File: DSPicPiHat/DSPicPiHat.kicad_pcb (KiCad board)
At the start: 2 copper layers, 65 x 66.5 mm, 85 parts, among them J1 Conn_01x09_Female, J4 Conn_PIC_ICSP_ICD, J5 USB_C_Receptacle_USB2.0, J6 PowerInput, J8 RasPiHeaders, SW1 POWER_Select, SW2 SW_DIP_x08, U1 DSPIC33CH512MP508T-I_PT, U10 DF5A6.2CJE_LM, U11 FT230XS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

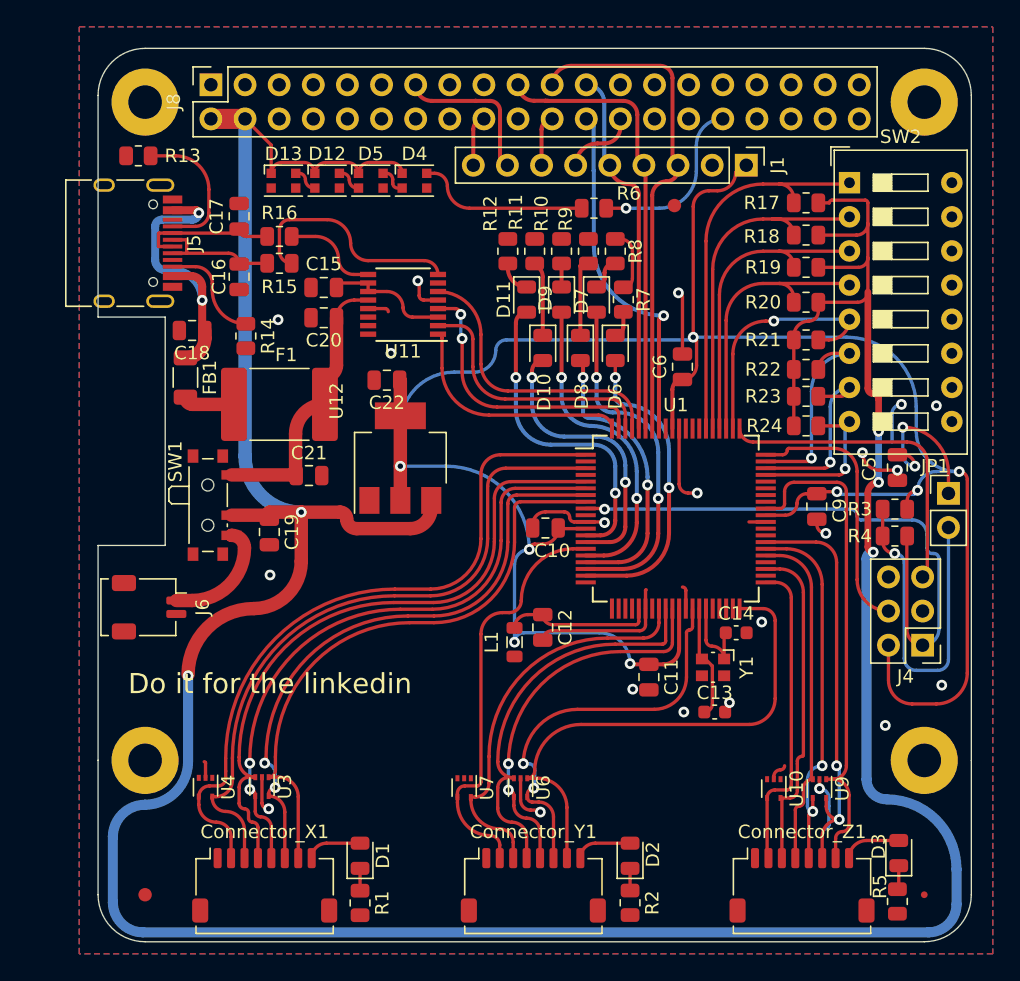
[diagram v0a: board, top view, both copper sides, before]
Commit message: Rounded some comers and added more pcb art
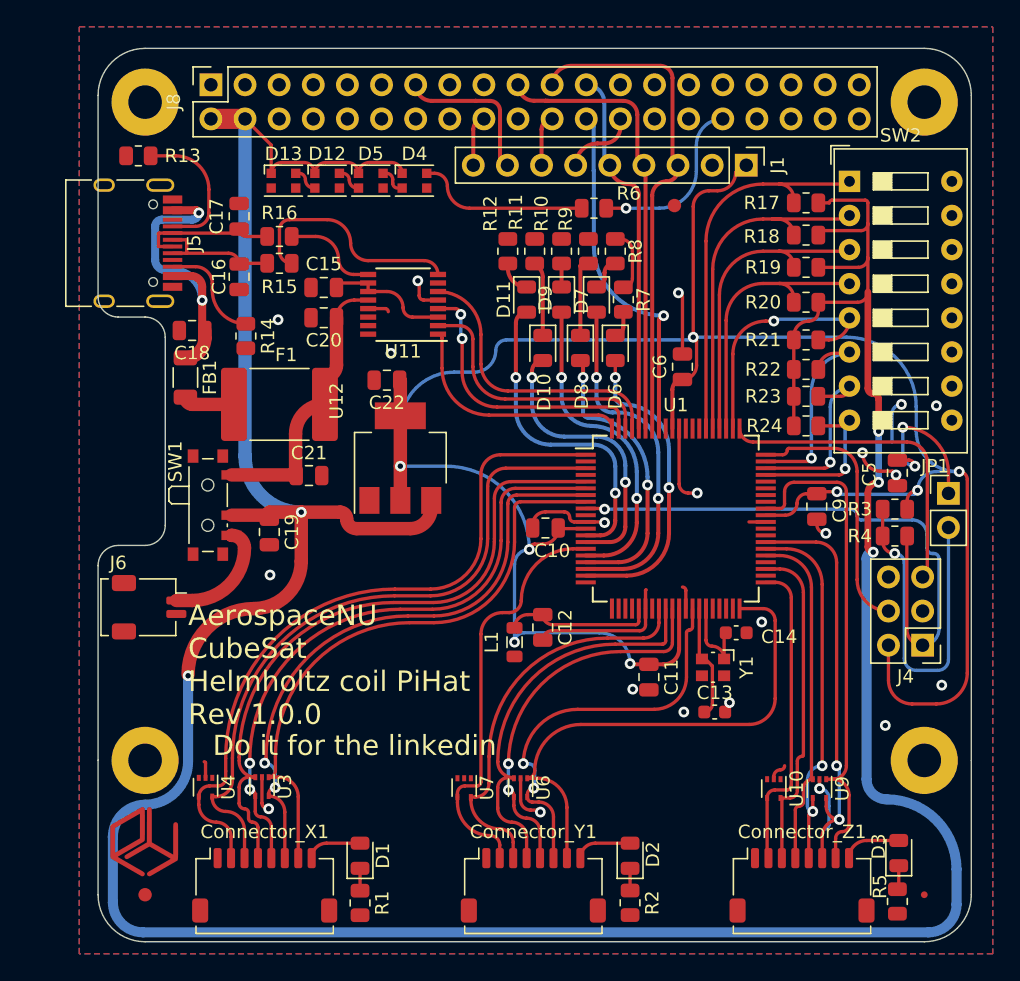
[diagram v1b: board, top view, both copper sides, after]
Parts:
- added G*** (x2): LOGO, footprints:SmallLogo, F.Cu at (60.0, 132.5)
- added G***: LOGO, footprints:Banner, B.Cu at (89.7, 134.0)
- moved C5 0.40 mm to (116.0, 105.1)
- moved SW2 0.10 mm to (112.4, 83.4)
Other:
- outline, holes or cut-outs redrawn
- board text added: "AerospaceNU CubeSat Helmholtz coil PiHat Rev 1.0.0"

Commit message: Grounded mounting points
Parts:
- removed ?: , 
- removed the REF** at (118.0, 77.5)
- removed the REF** at (60.0, 77.5)
- removed the REF** at (60.0, 126.5)
- added H1: MountingHole_Pad, MountingHole:MountingHole_2.7mm_M2.5_DIN965_Pad, F.Cu at (60.0, 77.5)
- added H2: MountingHole_Pad, MountingHole:MountingHole_2.7mm_M2.5_DIN965_Pad, F.Cu at (60.0, 126.5)
- added H3: MountingHole_Pad, MountingHole:MountingHole_2.7mm_M2.5_DIN965_Pad, F.Cu at (118.0, 126.5)
- added H4: MountingHole_Pad, MountingHole:MountingHole_2.7mm_M2.5_DIN965_Pad, F.Cu at (118.0, 77.5)
- moved C5 0.25 mm to (116.0, 105.3)
- moved R3 0.20 mm to (115.8, 108.0)
- moved R4 0.20 mm to (115.8, 110.0)

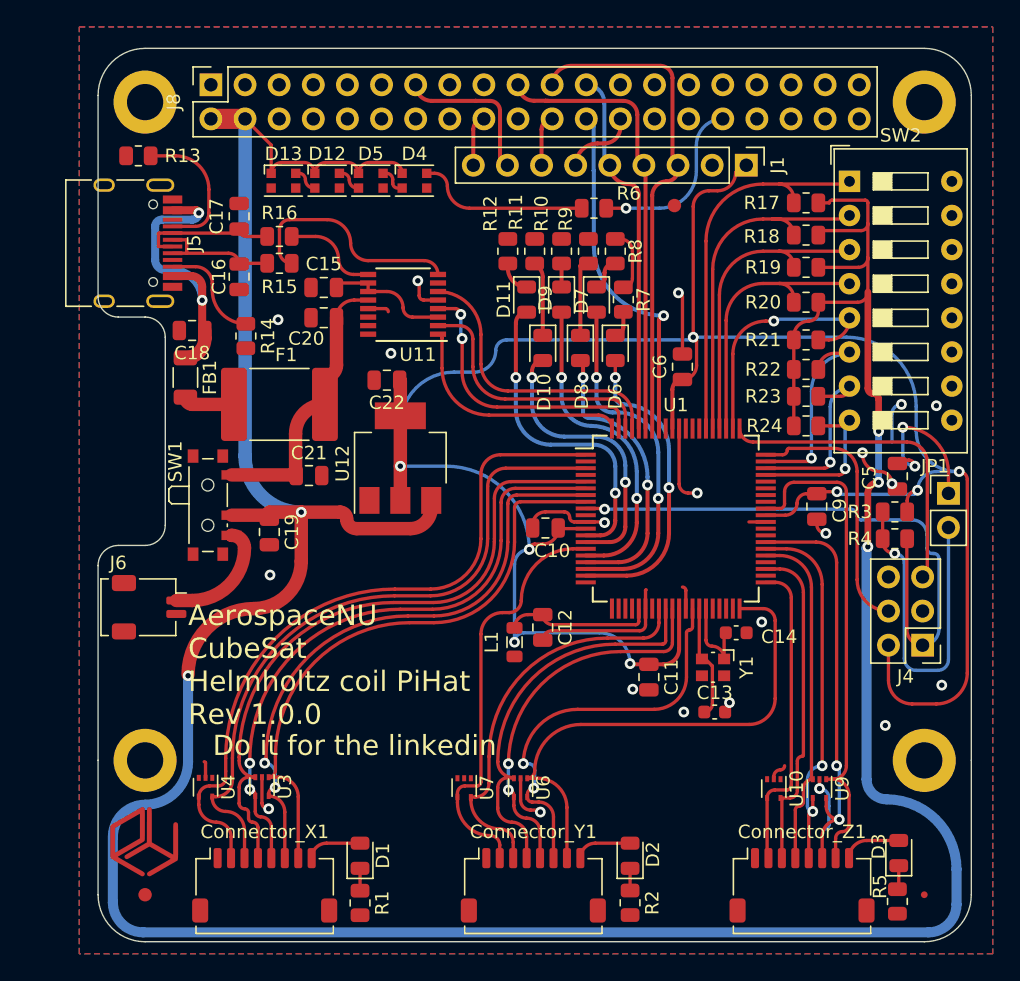
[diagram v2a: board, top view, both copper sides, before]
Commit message: Fixed pi header connections
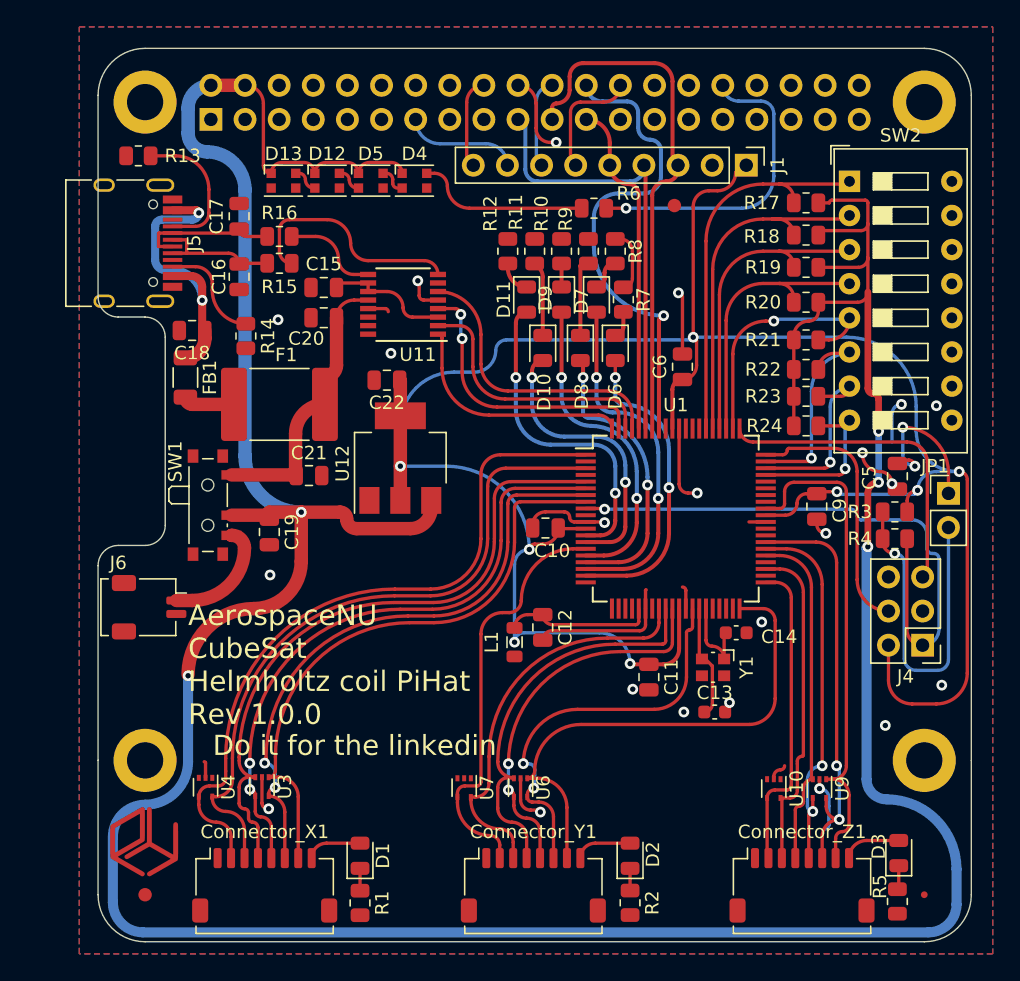
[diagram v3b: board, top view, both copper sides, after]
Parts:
- J8: moved to B.Cu
- moved J8 2.58 mm to (64.9, 78.8), turned to -90 degrees
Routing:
- net PI_NEOPIXEL: track 13.1 -> 23.3 mm
- net PI_CE0: track 26.2 -> 35.9 mm
- net +5V: track 252.7 -> 261.1 mm
- net AVSS: track 61.3 -> 67.2 mm, vias 21 -> 22
- net PI_CE1: track 5.45 -> 8.93 mm
- net Backlight: track 3.87 -> 6.89 mm
- net RST: track 11.6 -> 8.64 mm
- net Data/Command: track 3.87 -> 6.78 mm
- net PI_MISO: track 36.7 -> 39.0 mm
- net PI_SCLK: track 27.7 -> 26.5 mm

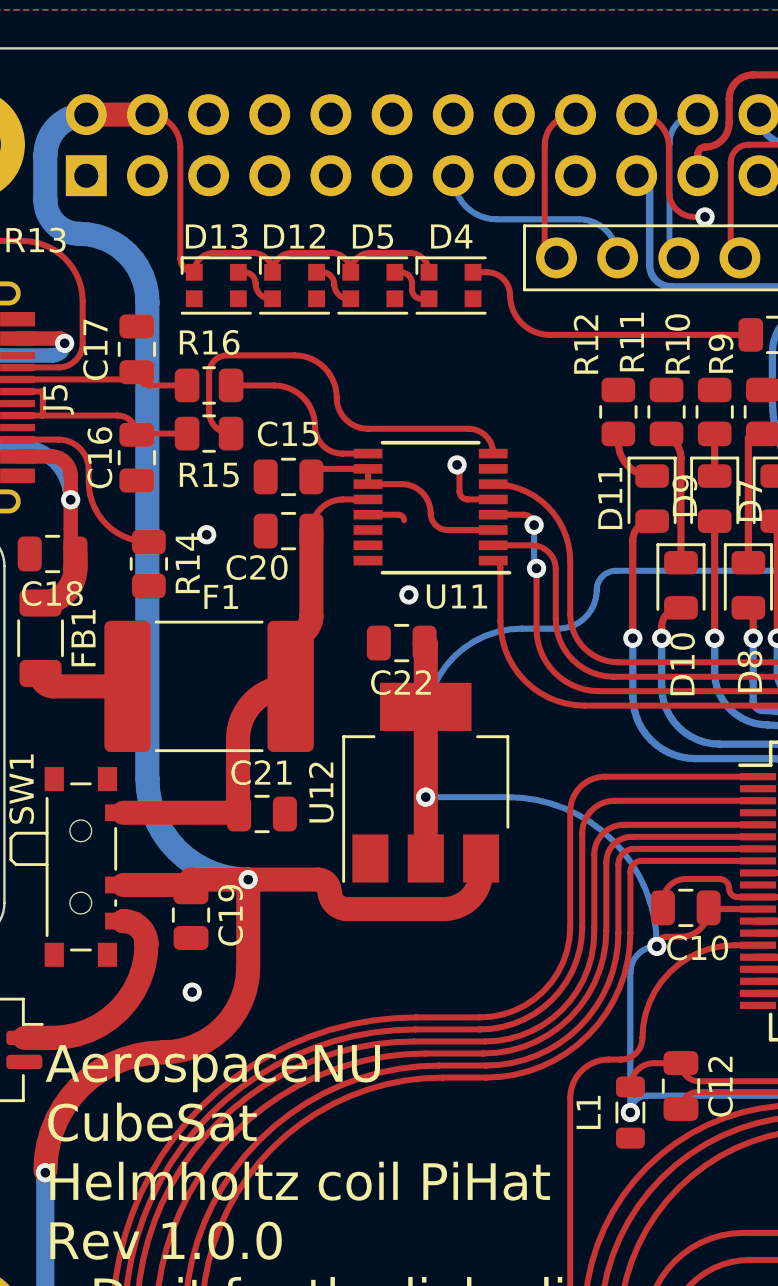
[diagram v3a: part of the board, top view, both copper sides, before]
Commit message: Moved fuse to be after the PSU switch
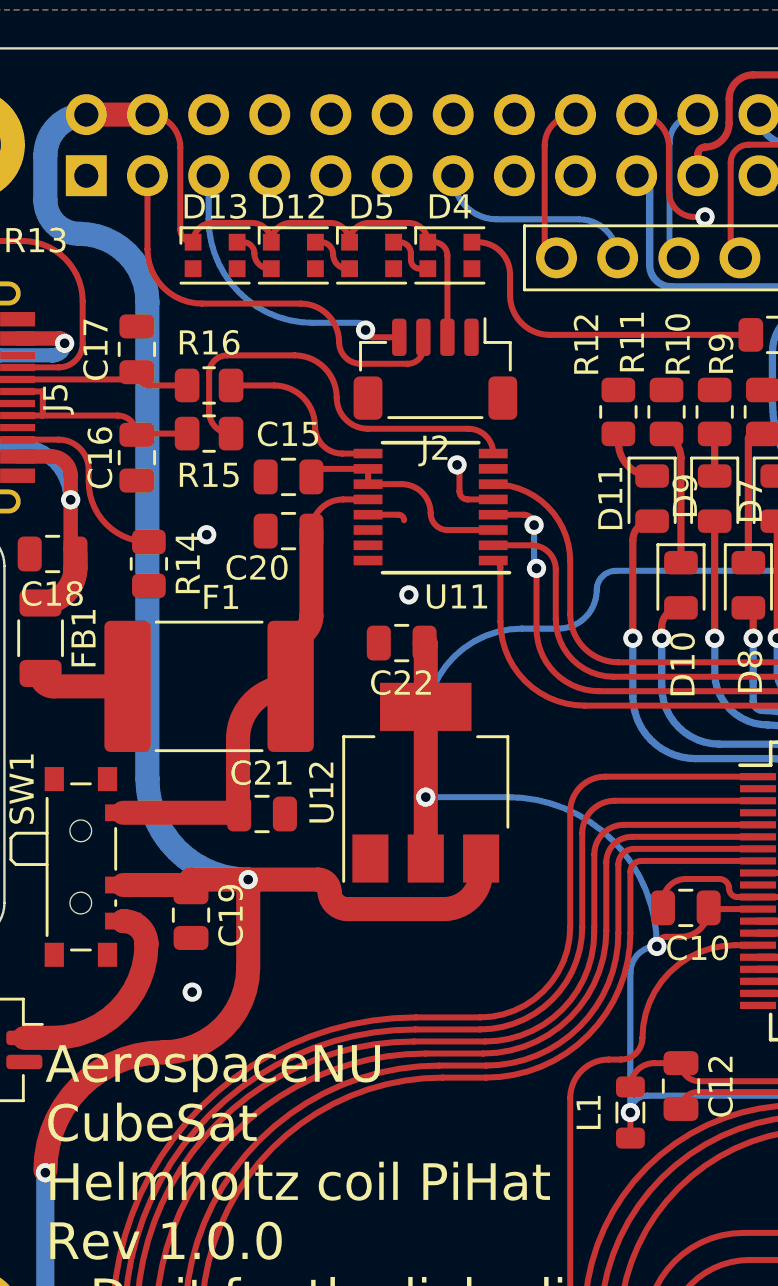
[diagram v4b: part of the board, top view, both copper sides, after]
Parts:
- added J2: Conn_01x04_Female, Connector_JST:JST_SH_BM04B-SRSS-TB_1x04-1MP_P1.00mm_Vertical, F.Cu at (79.4, 86.8)
- L1: value 10 mA <1o -> 6.33 mH
- moved D12 1.25 mm to (73.5, 82.1)
- moved D13 1.25 mm to (70.2, 82.1)
- moved D4 1.25 mm to (80.0, 82.1)
- moved D5 1.25 mm to (76.8, 82.1)
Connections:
- J8 pad 3: unconnected-(J8-Pad3) -> PI_I2C_SDA
- J8 pad 5: unconnected-(J8-Pad5) -> PI_I2C_SCL
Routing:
- net PI_I2C_SDA: track 0.00 -> 17.8 mm
- net PI_I2C_SCL: track 0.00 -> 12.3 mm, vias 0 -> 1
- net +5V: track 261.1 -> 264.3 mm
- net Net-(D4-Pad4): track 12.9 -> 14.0 mm
- net VDD: track 173.8 -> 174.9 mm

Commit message: oops
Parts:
- added TP1: TestPoint, TestPoint:TestPoint_Pad_D1.0mm, F.Cu at (52.9, 100.5)
- moved C21 8.50 mm to (64.6, 101.5), turned to 180 degrees
- moved F1 3.61 mm to (72.0, 103.0), turned to -90 degrees
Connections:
- F1 pad 1: Net-(F1-Pad1) -> Net-(SW1-Pad2)
- F1 pad 2: VBUS_USBC -> +5V
- FB1 pad 2: Net-(F1-Pad1) -> VBUS_USBC
- SW1 pad 2: +5V -> Net-(SW1-Pad2)
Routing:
- net Net-(SW1-Pad2): track 0.00 -> 11.6 mm
- net Net-(F1-Pad1): track 3.90 -> 0.00 mm
- net VBUS_USBC: track 21.5 -> 25.2 mm
- net +5V: track 264.3 -> 263.6 mm

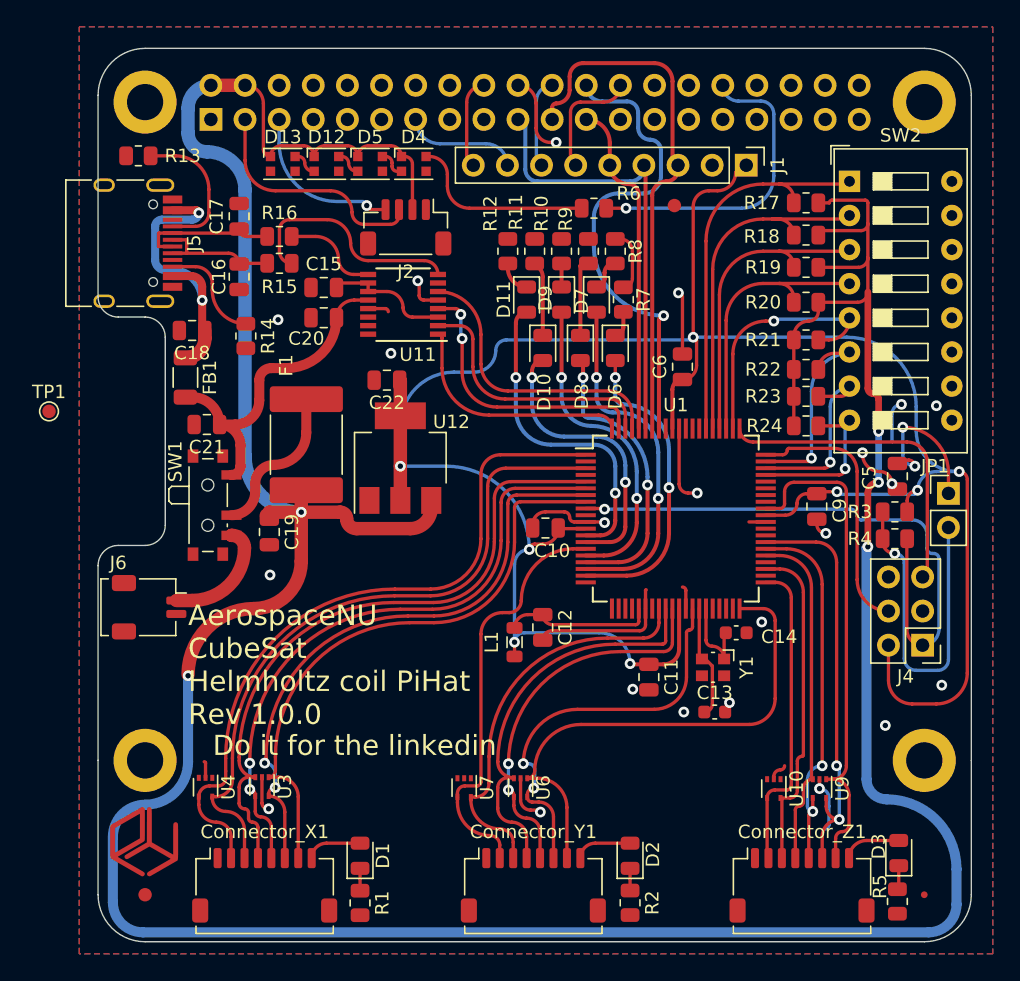
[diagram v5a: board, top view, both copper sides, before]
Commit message: added o ohm resistors based on braincodec's rx tx switcher
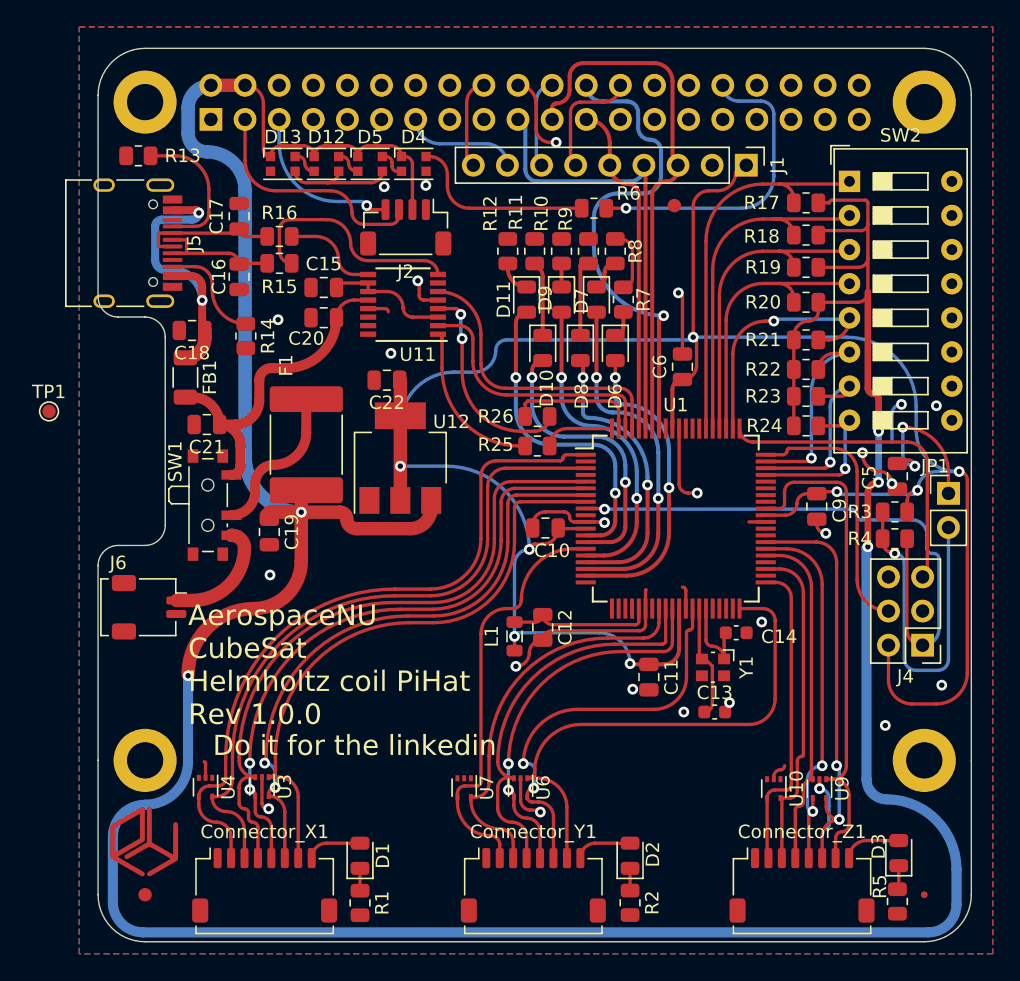
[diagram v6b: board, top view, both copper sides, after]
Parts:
- added R25: 0 o, Resistor_SMD:R_0805_2012Metric, F.Cu at (89.2, 103.1)
- added R26: 0 o, Resistor_SMD:R_0805_2012Metric, F.Cu at (89.2, 100.9)
- moved L1 0.43 mm to (87.5, 117.3)
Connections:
- U1 pad 79: U1RX -> Net-(U1-Pad79)
- U1 pad 80: U1TX -> Net-(U1-Pad80)
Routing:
- net AVSS: track 67.2 -> 79.0 mm, vias 22 -> 25
- net Net-(U1-Pad79): track 0.00 -> 9.69 mm
- net U1TX: track 17.7 -> 11.9 mm
- net Net-(U1-Pad80): track 0.00 -> 5.33 mm
- net U1RX: track 20.7 -> 15.8 mm
- net VDD: track 174.9 -> 174.2 mm
- net U1CTS: track 21.4 -> 21.9 mm

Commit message: dip_00 was unconnected, working through drc errors and warnings.
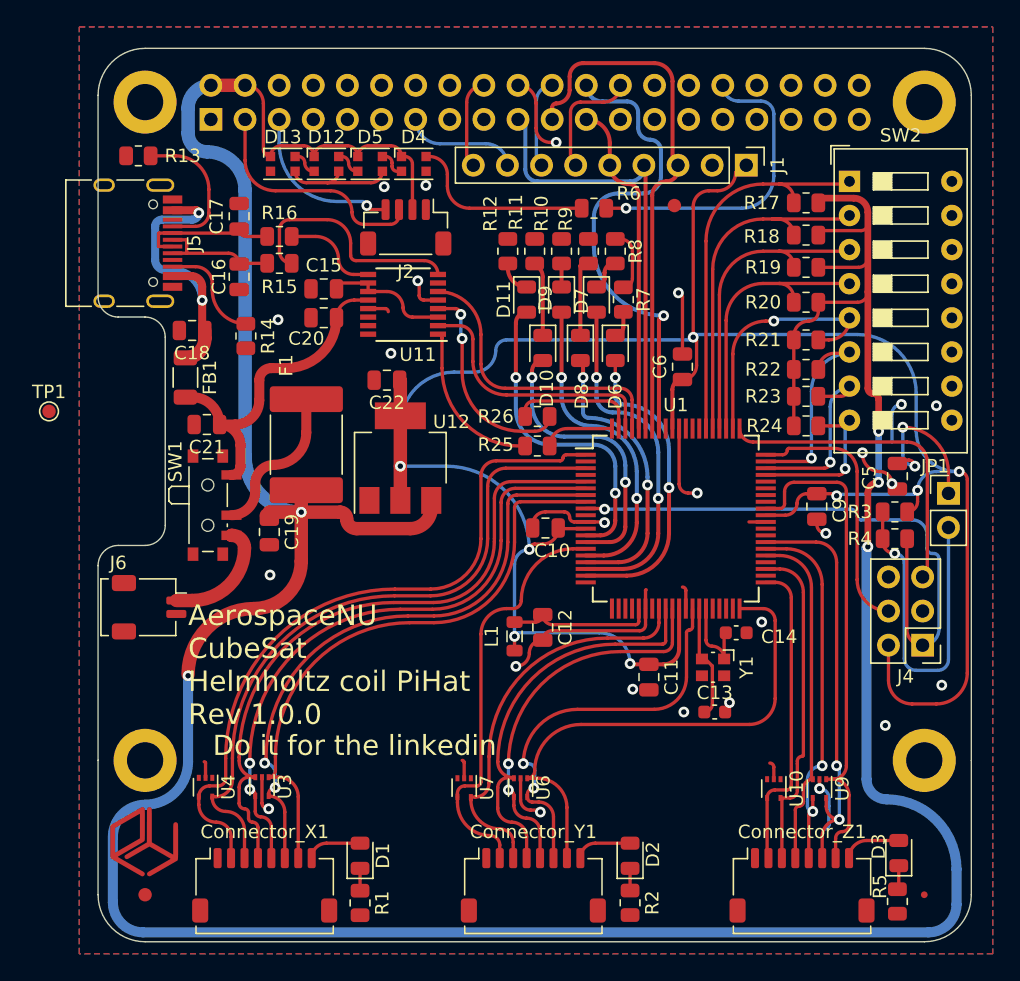
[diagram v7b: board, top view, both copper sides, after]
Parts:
- moved C15 0.10 mm to (73.3, 91.4)
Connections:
- U1 pad 66: unconnected-(U1-Pad66) -> DIP_00
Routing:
- net PI_SCLK: track 26.5 -> 25.1 mm
- net AVSS: track 79.0 -> 80.3 mm
- net VDD: track 174.2 -> 174.8 mm
